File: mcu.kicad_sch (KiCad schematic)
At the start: 41 parts, among them U1 STM32U5G9ZJTxQ, Y1 NX2016SA-16MHZ-EXS00A-CS07826, Y2 NX2012SA-32.768K-STD-MUB-1

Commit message: Fill the cartridge for all schematics
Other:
- company: (none) -> Julien Cruvieux
- title: (none) -> MCU
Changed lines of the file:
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@@
 	(paper "A3")
 	(title_block
-		(date "2025-11-01")
+		(title "MCU")
+		(date "2025-12-26")
+		(rev "A")
+		(company "Julien Cruvieux")
 	)
 	(rectangle

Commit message: Add footprints for inductors, missing one for L6
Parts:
- L1: footprint (none) -> Inductor_SMD:L_0805_2012Metric_Pad1.05x1.20mm_HandSolder
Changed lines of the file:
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@@
 			)
 		)
-		(property "Footprint" ""
+		(property "Footprint" "Inductor_SMD:L_0805_2012Metric_Pad1.05x1.20mm_HandSolder"
 			(at 121.92 199.39 0)
 			(effects
@@
 			)
 		)
-		(property "Datasheet" "~"
+		(property "Datasheet" "https://www.mouser.fr/datasheet/3/76/2/JELF243B_0040.pdf"
 			(at 121.92 199.39 0)
 			(effects

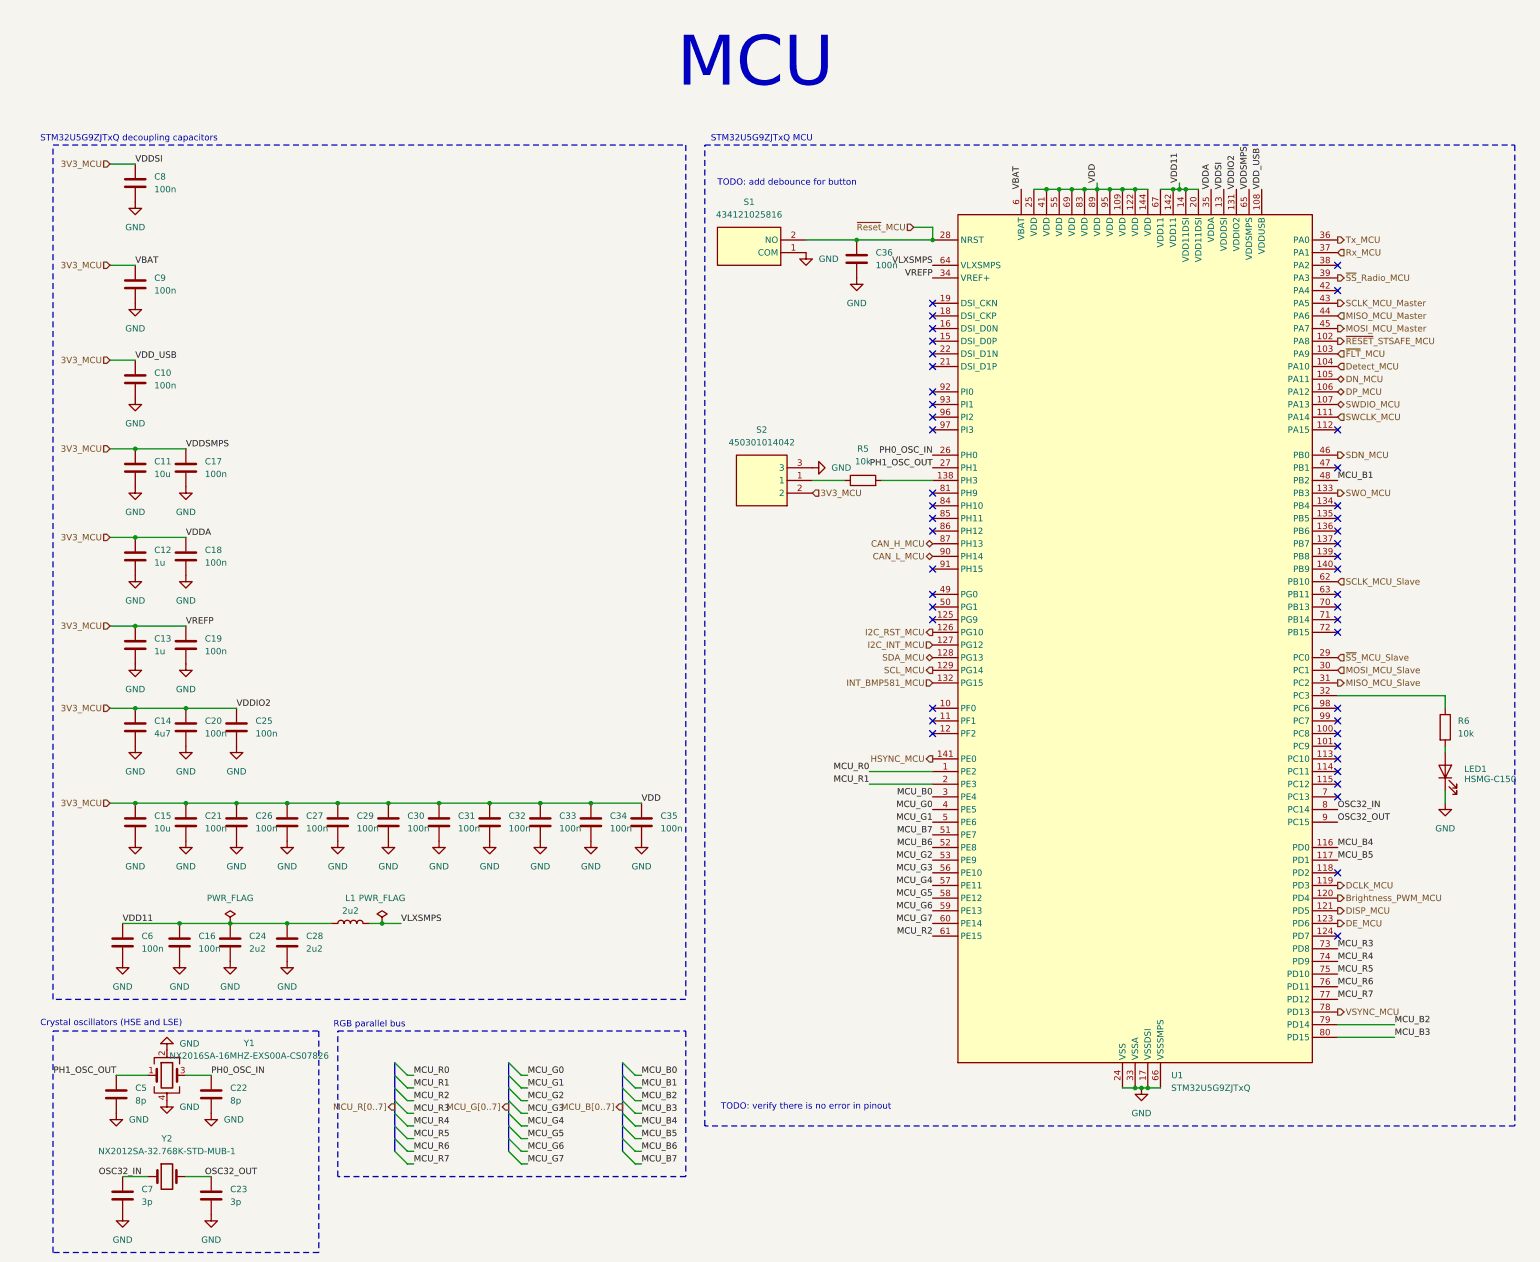
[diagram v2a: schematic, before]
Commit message: Components reindexing and update of PCB
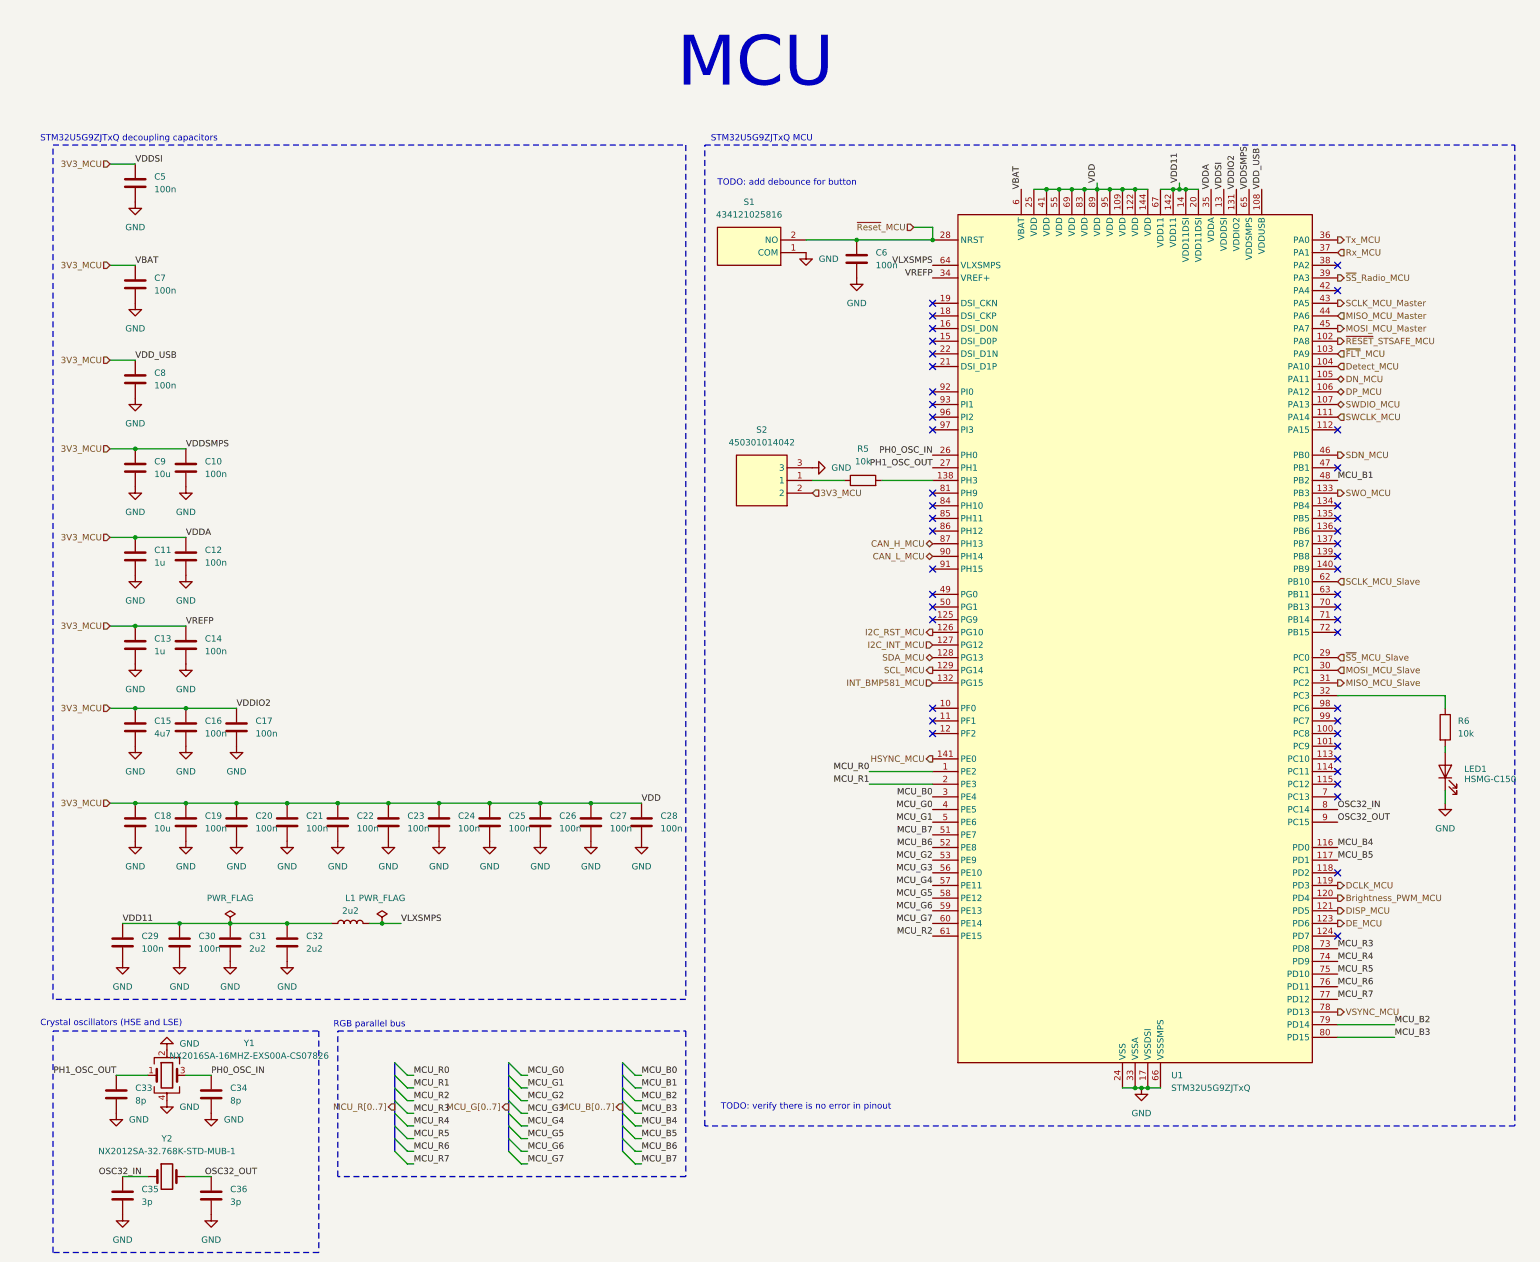
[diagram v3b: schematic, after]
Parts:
- renumbered C17 to C10, C12 to C11, C18 to C12, C19 to C14, C14 to C15, C20 to C16, C25 to C17, C15 to C18, C21 to C19, C26 to C20, C27 to C21, C29 to C22, C30 to C23, C31 to C24, C32 to C25, C33 to C26, C34 to C27, C35 to C28, C6 to C29, C16 to C30, C24 to C31, C28 to C32, C5 to C33, C22 to C34, C7 to C35, C23 to C36, C8 to C5, C36 to C6, C9 to C7, C10 to C8, C11 to C9
